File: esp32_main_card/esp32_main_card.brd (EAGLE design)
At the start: 100 x 80 mm, 11 parts, among them J1 09231486921, J2 USB3090-XX-X_REVE, U3 ESP32-DEVKITC-32D

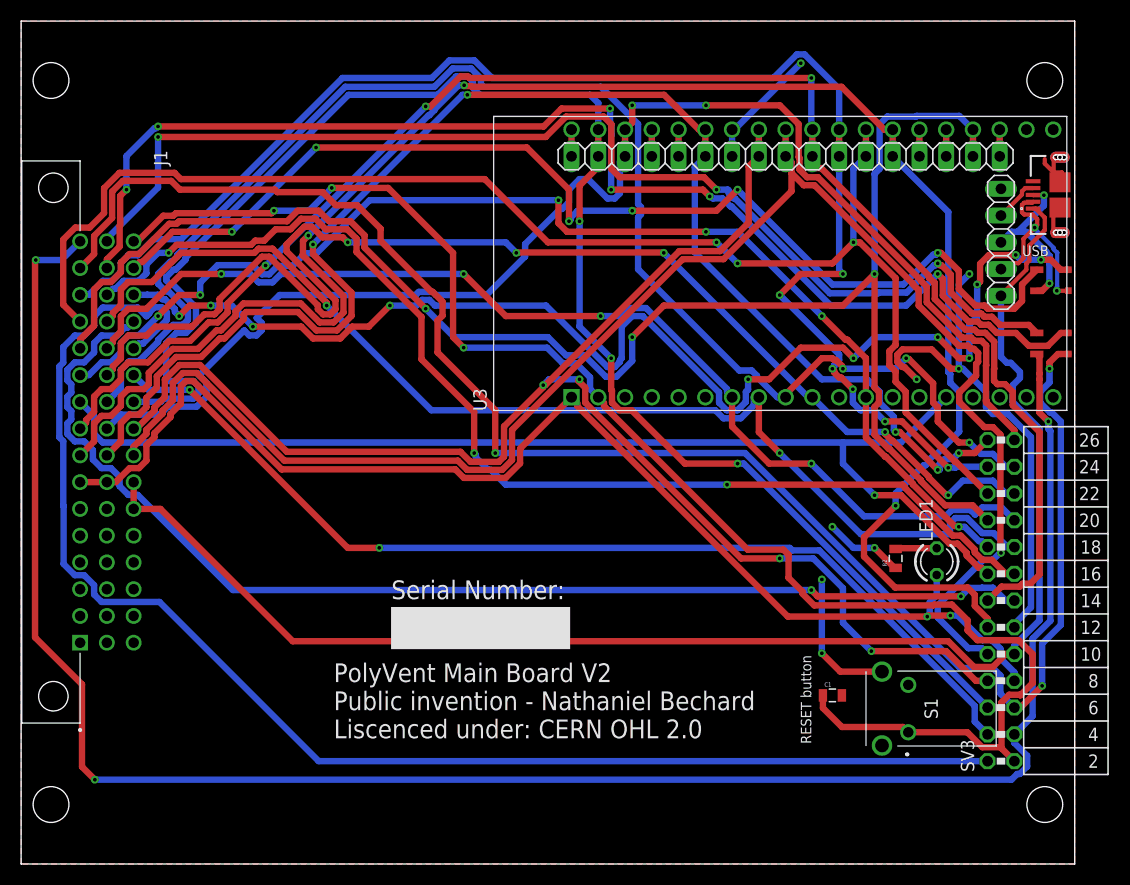
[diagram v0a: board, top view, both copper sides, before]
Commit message: updated libraries to generate better bom's
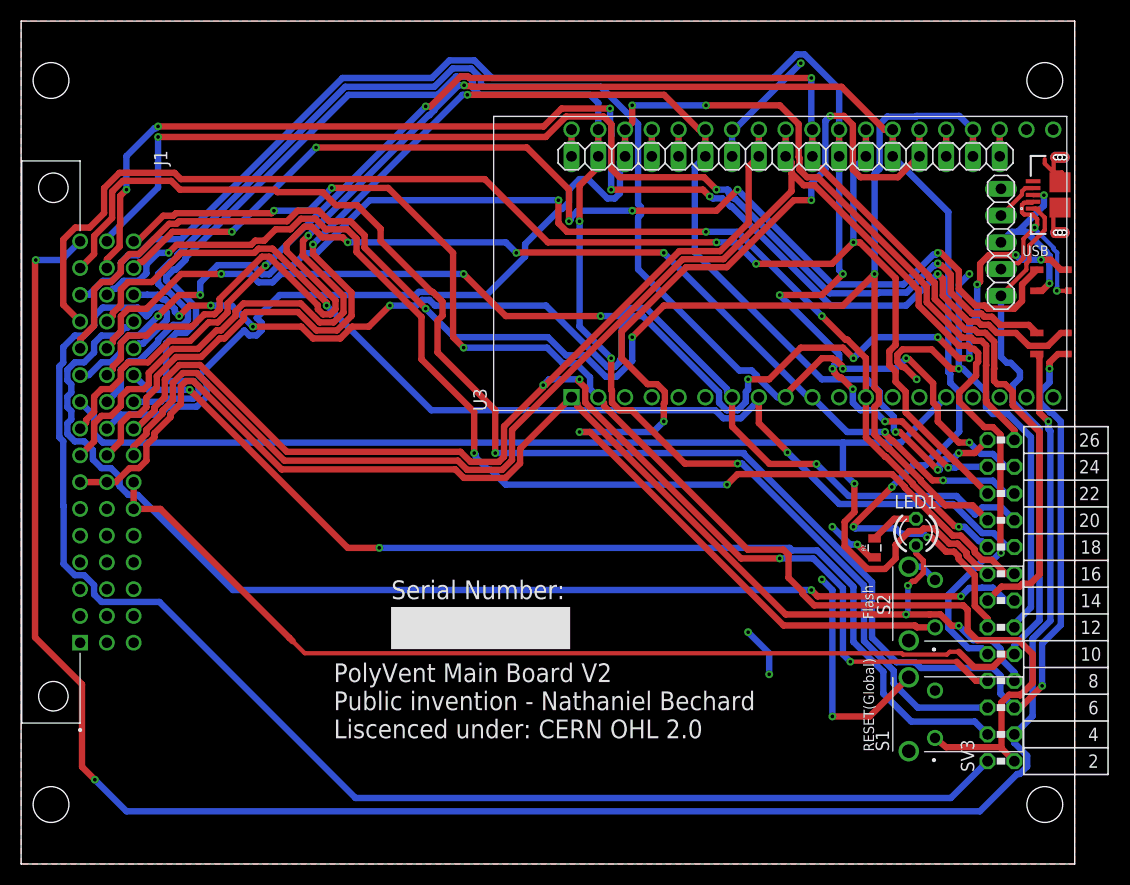
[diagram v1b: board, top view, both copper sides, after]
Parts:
- removed C1: 1 nf, SparkFun-Passives:0805
- added S2: FSMRA4JH04, FSMRA4JH04:FSMRA4JH04
- moved LED1 3.42 mm to (84.9, 31.5)
- moved R2 2.24 mm to (81.0, 30.0)
- moved S1 2.00 mm to (84.2, 14.5)
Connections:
- removed net N$5: JP1.4, U3.33
- new net IO0: JP1.4, S2.1, U3.33
- net GND: now also S2.2, S2.3, S2.4; no longer C1.2
- net RESET: no longer C1.1
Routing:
- net IO0: track 0.00 -> 109.3 mm, vias 0 -> 4
- net GND: track 90.2 -> 104.4 mm, vias 8 -> 10
- net RESET: track 145.6 -> 133.0 mm
- net CS_3: track 106.8 -> 116.0 mm
- net MOSI: track 151.8 -> 155.7 mm
- net SDA: track 96.0 -> 99.5 mm
- net 3.3V: track 119.4 -> 122.6 mm, vias 2 -> 3
- net USB1_D-: track 161.5 -> 164.6 mm
- net SCL: track 134.7 -> 137.6 mm
- net CS_13: track 107.8 -> 105.2 mm
- net N$5: track 2.54 -> 0.00 mm
- net USB1_D+: track 187.3 -> 189.8 mm
- net MISO: track 143.5 -> 145.3 mm
- net CS_1: track 169.6 -> 171.2 mm, vias 3 -> 5
- net CS_11: track 120.2 -> 119.1 mm
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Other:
- board text added: "Flash"
- board text added: "RESET(Global)"
- board text removed: "RESET button"

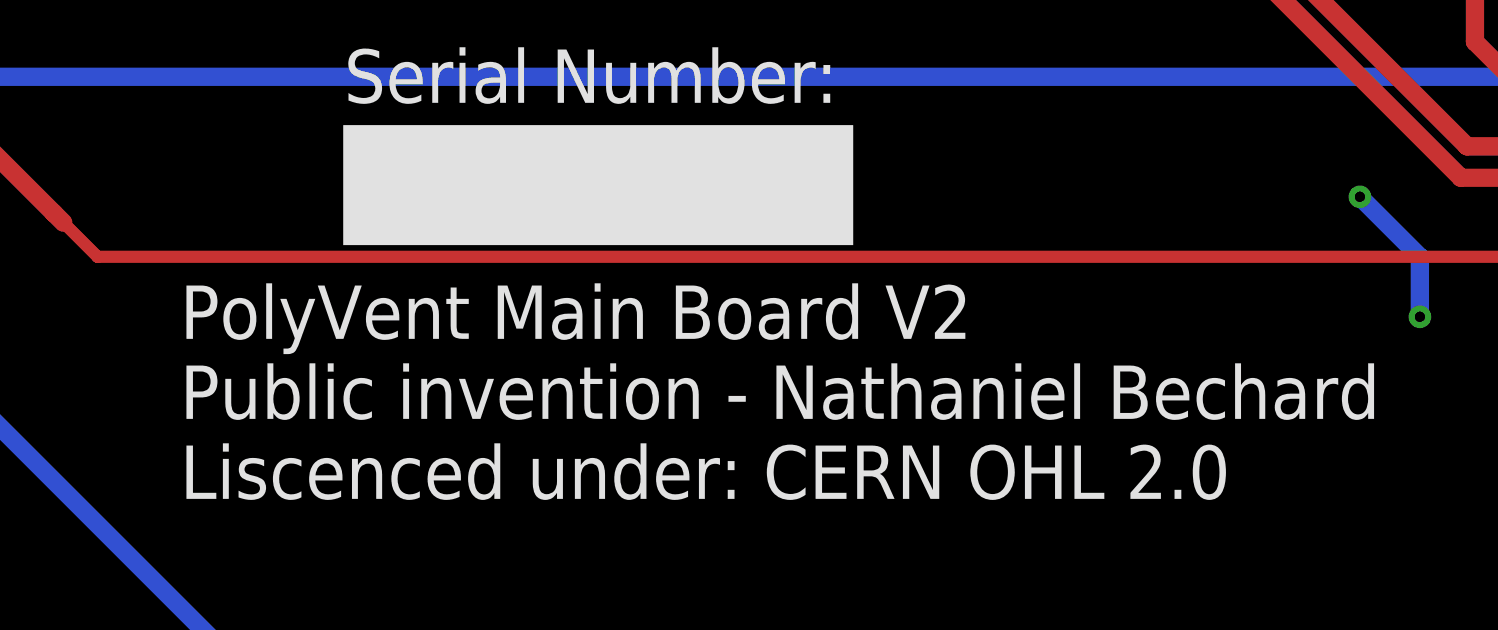
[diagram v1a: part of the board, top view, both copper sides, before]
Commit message: finished V2.2 control module update
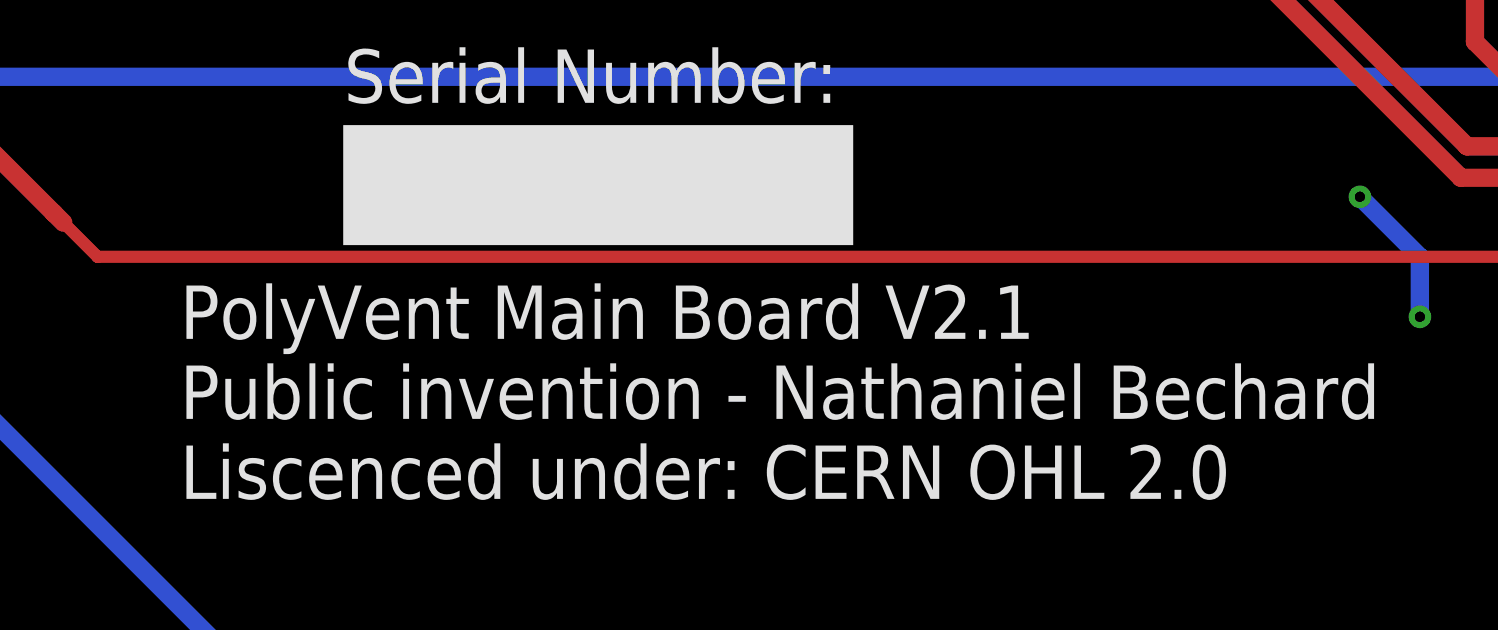
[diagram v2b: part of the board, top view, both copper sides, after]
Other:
- board text added: "PolyVent Main Board V2.1 Public invention - Nathaniel Bechard Liscenced under: CERN OHL 2.0"
- board text removed: "PolyVent Main Board V2 Public invention - Nathaniel Bechard Liscenced under: CERN OHL 2.0"
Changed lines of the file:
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@@
 <grid distance="1" unitdist="mm" unit="mm" style="lines" multiple="1" display="no" altdistance="0.01" altunitdist="mm" altunit="mm"/>
 <layers>
-<layer number="1" name="Top" color="4" fill="1" visible="yes" active="yes"/>
+<layer number="1" name="Top" color="4" fill="1" visible="no" active="yes"/>
 <layer number="2" name="Route2" color="16" fill="1" visible="no" active="no"/>
 <layer number="3" name="Route3" color="17" fill="1" visible="no" active="no"/>
@@
 <layer number="14" name="Route14" color="22" fill="1" visible="no" active="no"/>
 <layer number="15" name="Route15" color="23" fill="1" visible="no" active="no"/>
-<layer number="16" name="Bottom" color="1" fill="1" visible="yes" active="yes"/>
+<layer number="16" name="Bottom" color="1" fill="1" visible="no" active="yes"/>
 <layer number="17" name="Pads" color="2" fill="1" visible="yes" active="yes"/>
 <layer number="18" name="Vias" color="2" fill="1" visible="yes" active="yes"/>
@@
 </layers>
 <board>
-<fusionsync huburn="a.cGVyc29uYWw6dWUyYTJjODE0" projecturn="a.cGVyc29uYWw6dWUyYWFmMDMwIzIwMjAwODE1MzIzNjg3MzAx" f3durn="urn:adsk.wipprod:dm.lineage:MBjCJ3ZTQh-woY29vzdSqA" pcbguid="" lastpulledtime="" lastsyncedchangeguid="" latestrevisionid="dd28b56f-bde6-48a5-8226-f18c79e5ae6c" lastsyncedrevisionid="dd28b56f-bde6-48a5-8226-f18c79e5ae6c" lastboardhashguid="dedc9102-e237-7193-7661-bd02f836a8b0" lastpushedtime="2021-11-11T16:50:43Z" linktopcb3d="false"/>
+<fusionsync huburn="a.cGVyc29uYWw6dWUyYTJjODE0" projecturn="a.cGVyc29uYWw6dWUyYWFmMDMwIzIwMjAwODE1MzIzNjg3MzAx" f3durn="urn:adsk.wipprod:dm.lineage:MBjCJ3ZTQh-woY29vzdSqA" pcbguid="" lastpulledtime="" lastsyncedchangeguid="" latestrevisionid="dd28b56f-bde6-48a5-8226-f18c79e5ae6c" lastsyncedrevisionid="dd28b56f-bde6-48a5-8226-f18c79e5ae6c" lastboardhashguid="dedc9102-e237-7193-7661-bd02f836a8b0" lastpushedtime="2021-11-11T16:50:43Z" linktopcb3d="true"/>
 <plain>
 <wire x1="0" y1="0" x2="100" y2="0" width="0" layer="20"/>
@@
 <rectangle x1="41.61" y1="13.89" x2="45.61" y2="30.89" layer="25" rot="R90"/>
 <text x="51.6" y="26.91" size="1.778" layer="25" rot="R180">Serial Number:</text>
-<text x="29.67" y="11.93" size="1.778" layer="25">PolyVent Main Board V2
+<text x="29.67" y="11.93" size="1.778" layer="25">PolyVent Main Board V2.1
 Public invention - Nathaniel Bechard
 Liscenced under: CERN OHL 2.0</text>

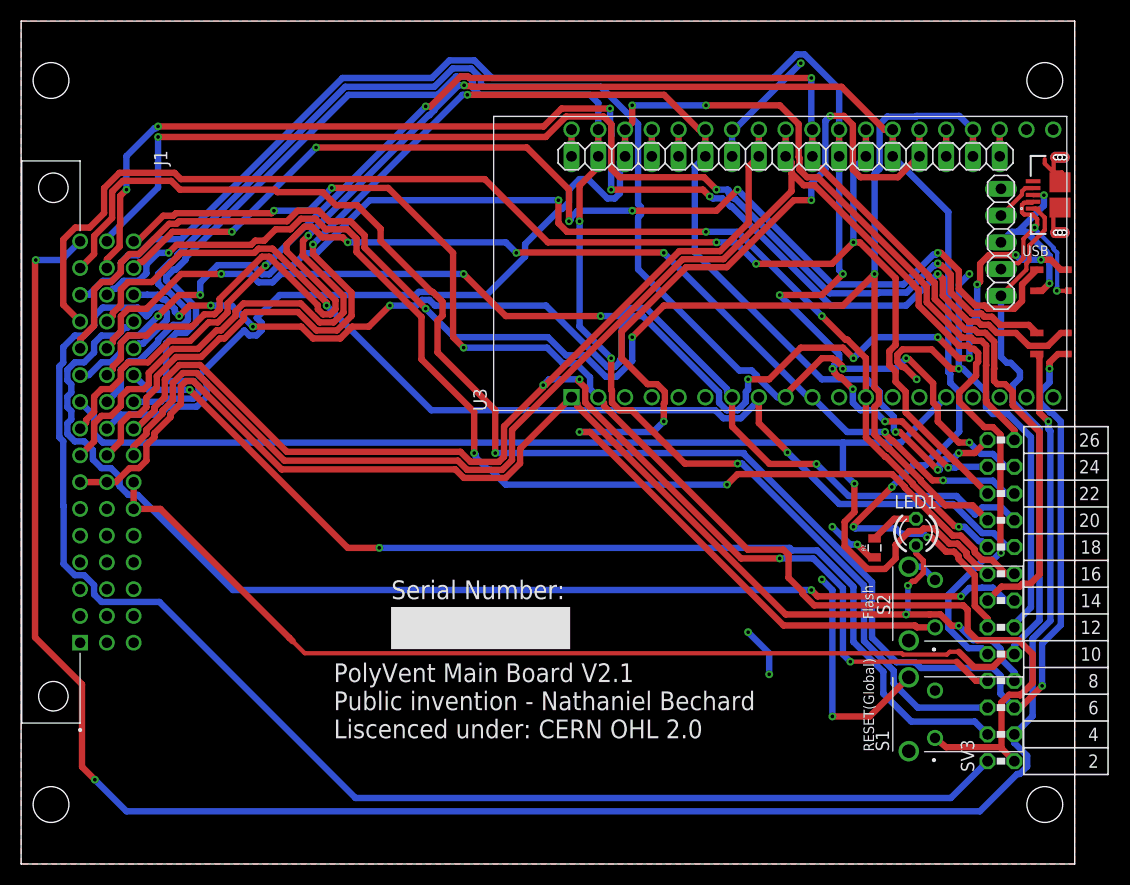
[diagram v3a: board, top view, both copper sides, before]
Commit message: added version 2.2 of the main board, which fixes the I2C pin problem
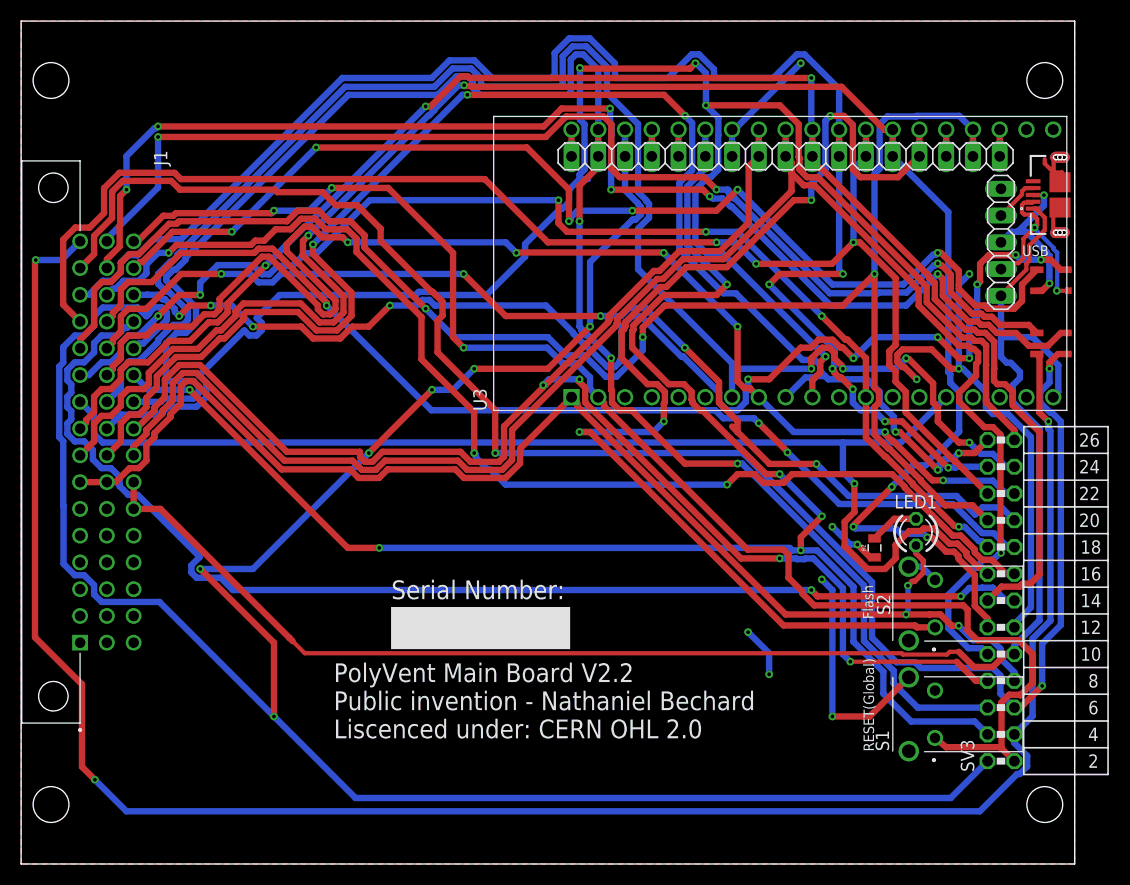
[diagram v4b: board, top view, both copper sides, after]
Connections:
- removed net N$10: U3.19
- net 5V: now also U3.19
- net CS_10: now also U3.7; no longer U3.9
- net CS_11: now also U3.8; no longer U3.10
- net CS_12: no longer U3.7
- net CS_13: no longer U3.8
- net CS_8: now also U3.9; no longer JP1.12, U3.25
- net CS_9: now also U3.10; no longer JP1.15, U3.22
- net SCL: now also JP1.15, U3.22
- net SDA: now also JP1.12, U3.25
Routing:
- net SCL: track 137.6 -> 222.5 mm, vias 0 -> 6
- net SDA: track 99.5 -> 158.4 mm, vias 2 -> 6
- net CS_9: track 130.6 -> 173.1 mm, vias 2 -> 4
- net 5V: track 141.4 -> 151.3 mm
- net CS_10: track 137.7 -> 147.2 mm, vias 3 -> 4
- net CS_7: track 138.4 -> 147.5 mm
- net MOSI: track 155.7 -> 162.8 mm
- net CS_8: track 136.6 -> 142.0 mm, vias 5 -> 6
- net CS_13: track 105.2 -> 101.9 mm, vias 2 -> 3
- net CS_11: track 119.1 -> 122.1 mm, vias 5 -> 6
- net CS_15: track 113.6 -> 115.5 mm
- net MISO: track 145.3 -> 146.7 mm
- net SCK: track 152.1 -> 153.2 mm
- net CS_12: track 103.4 -> 104.1 mm, vias 4 -> 5
- net CS_14: track 110.1 -> 110.8 mm
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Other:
- board text added: "PolyVent Main Board V2.2 Public invention - Nathaniel Bechard Liscenced under: CERN OHL 2.0"
- board text removed: "PolyVent Main Board V2.1 Public invention - Nathaniel Bechard Liscenced under: CERN OHL 2.0"
